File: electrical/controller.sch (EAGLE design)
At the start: 41 parts, among them IC1 555, IC2 MCP4728, Q1 DMP3098, Q2 N-CHANNEL-MOSFETSOT23-3, Q3 600mA/40V, Q4 DMP3098, U1 POLOLU_D24V22F5, U5 MCP6042, U6 MCP6042

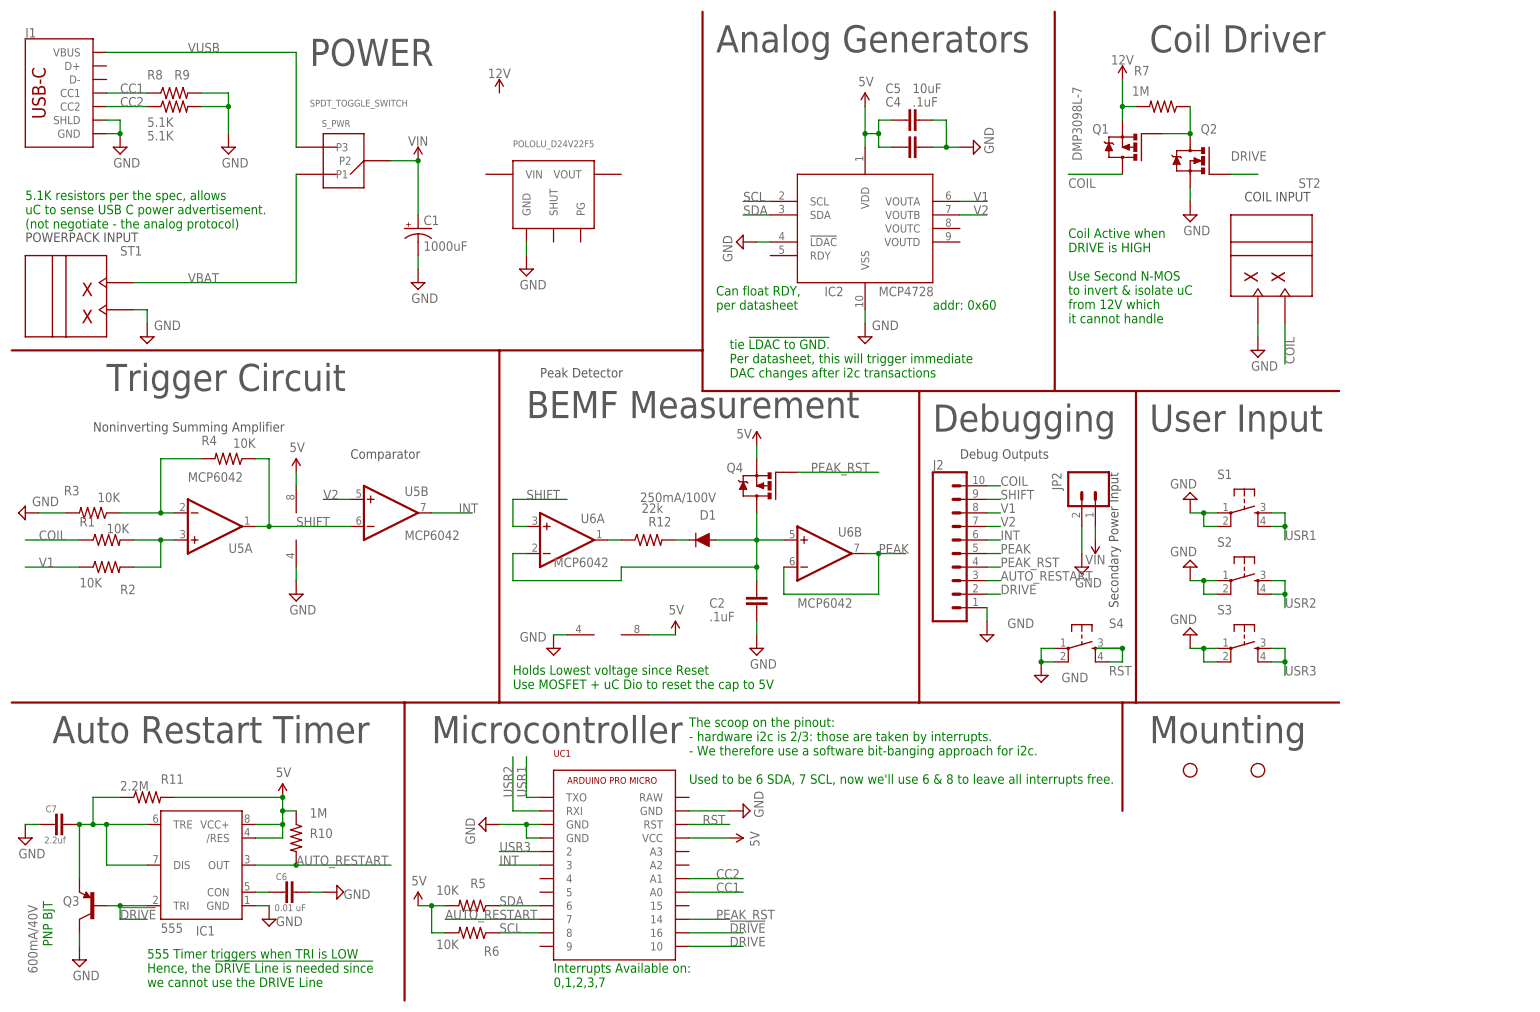
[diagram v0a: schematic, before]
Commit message: Most, but not all, of rev D2
Still need to test CC1 / CC2.
Add debug pinout silkscreen labels.
See if we can still use resistor arrays.
Calculate new values for the trigger op-amp network.
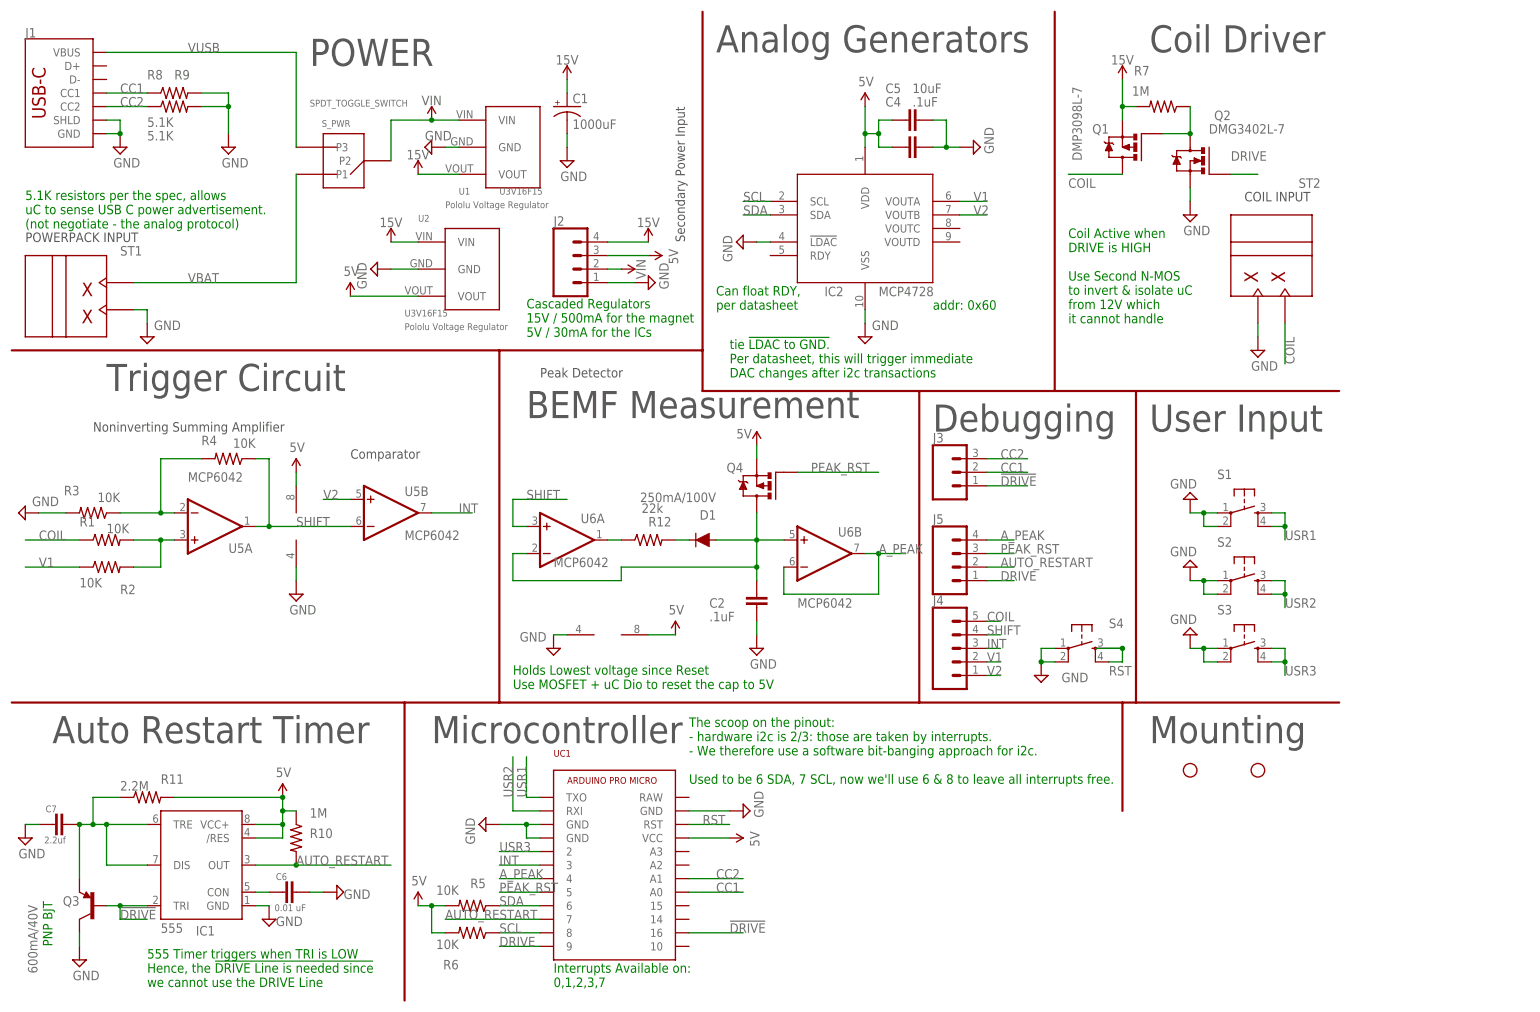
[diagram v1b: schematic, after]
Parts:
- removed JP2: (no value), pie:M02PTH
- added J3: 455-1750-1-ND, SparkFun-Connectors:CONN_03
- added J4: (no value), SparkFun-Connectors:CONN_05PTH
- added J5: (no value), SparkFun-Connectors:CONN_04PTH
- added U2: U3V16F15, BEST_Custom:POLOLU_VOLTAGE_REGULATOR_3PIN
- J2: device SparkFun-Connectors:CONN_10" -> SparkFun-Connectors:CONN_04PTH
- Q2: value N-CHANNEL-MOSFETSOT23-3 -> DMG3402L-7
- U1: value POLOLU_D24V22F5 -> U3V16F15; device BEST_Custom:POLOLU_D24V22F5 -> BEST_Custom:POLOLU_VOLTAGE_REGULATOR_3PINBOOST
- UC1: value ARDUINO_PRO_MICRO -> (none); device BEST_Custom:ARDUINO_PRO_MICRO -> BEST_Custom:ARDUINO_PRO_MICRO2D
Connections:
- removed net 12V: Q1.S, R7.2
- removed net PEAK: J2.5, U6B.-IN, U6B.OUT
- new net 15V: C1.+, J2.4, Q1.S, R7.2, U1.VOUT, U2.VIN
- new net A_PEAK: J5.4, U6B.-IN, U6B.OUT, UC1.4
- net !DRIVE: now also J3.1
- net 5V: now also J2.3, U2.VOUT
- net AUTO_RESTART: now also J5.2; no longer J2.3
- net CC1: now also J3.2
- net CC2: now also J3.3
- net COIL: now also J4.5; no longer J2.10
- net DRIVE: now also J5.1, UC1.9; no longer J2.2, UC1.10
- net GND: now also U2.GND; no longer JP2.2
- net INT: now also J4.3; no longer J2.6
- net PEAK_RST: now also J5.3, UC1.5; no longer J2.4, UC1.14
- net SHIFT: now also J4.4; no longer J2.9
- net V1: now also J4.2; no longer J2.8
- net V2: now also J4.1; no longer J2.7
- net VIN: now also J2.2, U1.VIN; no longer C1.+, JP2.1
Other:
- note added: "Cascaded Regulators 15V / 500mA for the magnet 5V / 30mA for the ICs"
- note removed: "Debug Outputs"
- note removed: "TODO: CAD & add the 12V / 5V regulators Pololu D45V1E1F5 and U3V16F12"
- moved on the sheet: C1

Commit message: Calculate resistor values for new coil
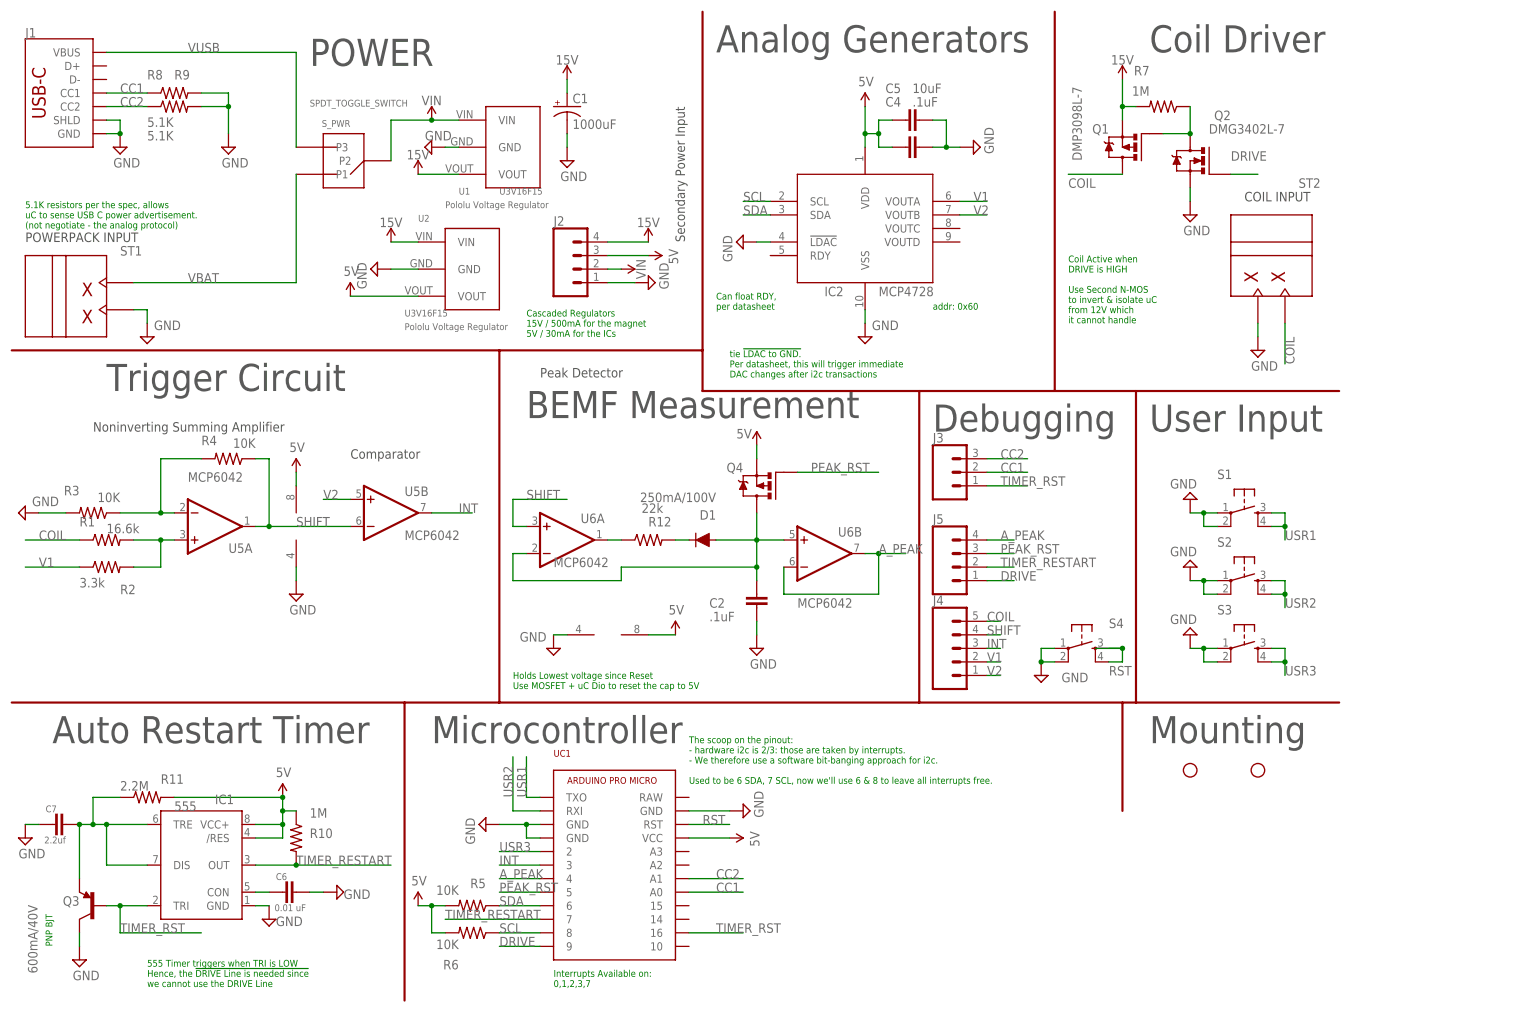
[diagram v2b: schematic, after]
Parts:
- R1: value 10K -> 16.6k
- R2: value 10K -> 3.3k
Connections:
- net !DRIVE renamed TIMER_RST
- net AUTO_RESTART renamed TIMER_RESTART
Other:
- note added: "Stage 1: V+ = R1*V1 + R2*Vcoil / (R1 + R2) Choose R1+R2 = 10k. Solve for Values by solving simultaneous equations: 1) Set Coil = 0, choose V+ = 1V ==> VShift = 2V 2) Set Coil = 3, choose V+ = 1.5V ==> VShift = 3V Previous 5V coil operation chose Coil = 1, V+ = 1.5 (approx 3x the coil count, 1/3 the gain) (Actually it's 2.69x the coil count, todo adjust later)"
- note added: "Stage 2: VShift = 1 + (R4/R3) V- VShift = 2 V-"
- note removed: "TODO: Gain math for Coil to reduce the BEMF by 3x"
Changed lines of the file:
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@@
 <part name="SUPPLY5" library="pie" deviceset="GND" device=""/>
 <part name="SUPPLY6" library="pie" deviceset="GND" device=""/>
-<part name="R2" library="pie" deviceset="R-US_" device="R0603" value="10K"/>
+<part name="R2" library="pie" deviceset="R-US_" device="R0603" value="3.3k"/>
 <part name="R3" library="pie" deviceset="R-US_" device="R0603" value="10K"/>
 <part name="R4" library="pie" deviceset="R-US_" device="R0603" value="10K"/>
@@
 <part name="U$4" library="pie" deviceset="5V" device=""/>
 <part name="SUPPLY8" library="pie" deviceset="GND" device=""/>
-<part name="R1" library="pie" deviceset="R-US_" device="R0603" value="10K"/>
+<part name="R1" library="pie" deviceset="R-US_" device="R0603" value="16.6k"/>
 <part name="SUPPLY10" library="pie" deviceset="GND" device=""/>
 <part name="C5" library="pie" deviceset="CAP" device="0805" value="10uF"/>
@@
 <wire x1="91.44" y1="55.88" x2="170.18" y2="55.88" width="0.4064" layer="94"/>
 <text x="213.36" y="48.26" size="5.08" layer="97">Mounting</text>
-<text x="101.6" y="2.54" size="1.778" layer="91">Interrupts Available on:
+<text x="101.6" y="2.54" size="1.27" layer="91">Interrupts Available on:
 0,1,2,3,7</text>
-<text x="127" y="40.64" size="1.778" layer="91">The scoop on the pinout:
+<text x="127" y="40.64" size="1.27" layer="91">The scoop on the pinout:
 - hardware i2c is 2/3: those are taken by interrupts.
 - We therefore use a software bit-banging approach for i2c.
 Used to be 6 SDA, 7 SCL, now we'll use 6 &amp; 8 to leave all interrupts free.</text>
-<text x="172.72" y="129.54" size="1.778" layer="91">addr: 0x60</text>
-<text x="2.54" y="144.78" size="1.778" layer="91">5.1K resistors per the spec, allows
+<text x="172.72" y="129.54" size="1.27" layer="91">addr: 0x60</text>
+<text x="2.54" y="144.78" size="1.27" layer="91">5.1K resistors per the spec, allows
 uC to sense USB C power advertisement.
 (not negotiate - the analog protocol)</text>
-<text x="7.62" y="10.16" size="1.778" layer="91" rot="R90">PNP BJT</text>
-<text x="134.62" y="116.84" size="1.778" layer="91">tie !LDAC to GND.
+<text x="7.62" y="10.16" size="1.27" layer="91" rot="R90">PNP BJT</text>
+<text x="134.62" y="116.84" size="1.27" layer="91">tie !LDAC to GND.
 Per datasheet, this will trigger immediate
 DAC changes after i2c transactions</text>
-<text x="132.08" y="129.54" size="1.778" layer="91">Can float RDY,
+<text x="132.08" y="129.54" size="1.27" layer="91">Can float RDY,
 per datasheet</text>
 <text x="200.66" y="157.48" size="1.778" layer="96" rot="R90">DMP3098L-7</text>
-<text x="198.12" y="127" size="1.778" layer="91">Coil Active when
+<text x="198.12" y="127" size="1.27" layer="91">Coil Active when
 DRIVE is HIGH
 Use Second N-MOS
@@
 from 12V which
 it cannot handle</text>
-<text x="25.4" y="2.54" size="1.778" layer="91">555 Timer triggers when TRI is LOW
+<text x="25.4" y="2.54" size="1.27" layer="91">555 Timer triggers when TRI is LOW
 Hence, the !DRIVE Line is needed since
 we cannot use the DRIVE Line</text>
@@
 <wire x1="195.58" y1="114.3" x2="195.58" y2="185.42" width="0.4064" layer="94"/>
 <text x="99.06" y="116.84" size="1.778" layer="97">Peak Detector</text>
-<text x="93.98" y="58.42" size="1.778" layer="91">Holds Lowest voltage since Reset
+<text x="93.98" y="58.42" size="1.27" layer="91">Holds Lowest voltage since Reset
 Use MOSFET + uC Dio to reset the cap to 5V</text>
-<text x="17.78" y="60.96" size="1.778" layer="98">TODO: Gain math for Coil to reduce the BEMF by 3x</text>
-<text x="96.52" y="124.46" size="1.778" layer="91">Cascaded Regulators
+<text x="2.54" y="58.42" size="1.27" layer="98">Stage 1:
+V+ = R1*V1 + R2*Vcoil / (R1 + R2)
+Choose R1+R2 = 10k.  Solve for Values by
+solving simultaneous equations:
+1) Set Coil = 0, choose V+ = 1V ==&gt; VShift = 2V
+2) Set Coil = 3, choose V+ = 1.5V ==&gt; VShift = 3V
+Previous 5V coil operation chose Coil = 1, V+ = 1.5 (approx 3x the coil count, 1/3 the gain)
+(Actually it's 2.69x the coil count, todo adjust later)</text>
+<text x="96.52" y="124.46" size="1.27" layer="91">Cascaded Regulators
 15V / 500mA for the magnet
 5V / 30mA for the ICs</text>
+<text x="33.02" y="76.2" size="1.27" layer="98">Stage 2:
+VShift = 1 + (R4/R3) V-
+VShift = 2 V-</text>
 </plain>
 <instances>
@@
 </instance>
 <instance part="IC1" gate="G$1" x="35.56" y="25.4" smashed="yes">
-<attribute name="NAME" x="38.1" y="13.97" size="1.778" layer="95" rot="R180"/>
-<attribute name="VALUE" x="27.94" y="12.7" size="1.778" layer="96"/>
+<attribute name="NAME" x="38.1" y="36.83" size="1.778" layer="95"/>
+<attribute name="VALUE" x="30.48" y="35.56" size="1.778" layer="96"/>
 </instance>
 <instance part="U$8" gate="G$1" x="50.8" y="38.1" smashed="yes">
@@
 <pinref part="C6" gate="G$1" pin="1"/>
 <wire x1="45.72" y1="20.32" x2="48.26" y2="20.32" width="0.1524" layer="91"/>
-</segment>
-</net>
-<net name="AUTO_RESTART" class="0">
-<segment>
-<pinref part="IC1" gate="G$1" pin="OUT"/>
-<wire x1="45.72" y1="25.4" x2="53.34" y2="25.4" width="0.1524" layer="91"/>
-<label x="53.34" y="25.4" size="1.778" layer="95"/>
-<pinref part="R10" gate="G$1" pin="2"/>
-<wire x1="53.34" y1="25.4" x2="71.12" y2="25.4" width="0.1524" layer="91"/>
-<junction x="53.34" y="25.4"/>
-</segment>
-<segment>
-<pinref part="UC1" gate="APM" pin="7"/>
-<wire x1="99.06" y1="15.24" x2="81.28" y2="15.24" width="0.1524" layer="91"/>
-<label x="81.28" y="15.24" size="1.778" layer="95"/>
-</segment>
-<segment>
-<wire x1="182.88" y1="81.28" x2="187.96" y2="81.28" width="0.1524" layer="91"/>
-<label x="185.42" y="81.28" size="1.778" layer="95"/>
-<pinref part="J5" gate="J1" pin="2"/>
 </segment>
 </net>
@@
 <wire x1="15.24" y1="33.02" x2="15.24" y2="38.1" width="0.1524" layer="91"/>
 <wire x1="15.24" y1="38.1" x2="20.32" y2="38.1" width="0.1524" layer="91"/>
-</segment>
-</net>
-<net name="!DRIVE" class="0">
-<segment>
-<pinref part="UC1" gate="APM" pin="16"/>
-<wire x1="127" y1="12.7" x2="137.16" y2="12.7" width="0.1524" layer="91"/>
-<label x="134.62" y="12.7" size="1.778" layer="95"/>
-</segment>
-<segment>
-<pinref part="IC1" gate="G$1" pin="TRI"/>
-<wire x1="20.32" y1="17.78" x2="25.4" y2="17.78" width="0.1524" layer="91"/>
-<label x="20.32" y="15.24" size="1.778" layer="95"/>
-<wire x1="20.32" y1="17.78" x2="20.32" y2="15.24" width="0.1524" layer="91"/>
-<wire x1="20.32" y1="15.24" x2="25.4" y2="15.24" width="0.1524" layer="91"/>
-<pinref part="Q3" gate="G$1" pin="B"/>
-<wire x1="20.32" y1="17.78" x2="17.78" y2="17.78" width="0.1524" layer="91"/>
-<junction x="20.32" y="17.78"/>
-</segment>
-<segment>
-<pinref part="J3" gate="J1" pin="1"/>
-<wire x1="182.88" y1="96.52" x2="190.5" y2="96.52" width="0.1524" layer="91"/>
-<label x="185.42" y="96.52" size="1.778" layer="95"/>
 </segment>
 </net>
@@
 </segment>
 </net>
+<net name="TIMER_RST" class="0">
+<segment>
+<pinref part="UC1" gate="APM" pin="16"/>
+<wire x1="127" y1="12.7" x2="137.16" y2="12.7" width="0.1524" layer="91"/>
+<label x="132.08" y="12.7" size="1.778" layer="95"/>
+</segment>
+<segment>
+<pinref part="IC1" gate="G$1" pin="TRI"/>
+<wire x1="20.32" y1="17.78" x2="25.4" y2="17.78" width="0.1524" layer="91"/>
+<label x="20.32" y="12.7" size="1.778" layer="95"/>
+<wire x1="20.32" y1="17.78" x2="20.32" y2="12.7" width="0.1524" layer="91"/>
+<wire x1="20.32" y1="12.7" x2="35.56" y2="12.7" width="0.1524" layer="91"/>
+<pinref part="Q3" gate="G$1" pin="B"/>
+<wire x1="20.32" y1="17.78" x2="17.78" y2="17.78" width="0.1524" layer="91"/>
+<junction x="20.32" y="17.78"/>
+</segment>
+<segment>
+<pinref part="J3" gate="J1" pin="1"/>
+<wire x1="182.88" y1="96.52" x2="190.5" y2="96.52" width="0.1524" layer="91"/>
+<label x="185.42" y="96.52" size="1.778" layer="95"/>
+</segment>
+</net>
+<net name="TIMER_RESTART" class="0">
+<segment>
+<pinref part="IC1" gate="G$1" pin="OUT"/>
+<wire x1="45.72" y1="25.4" x2="53.34" y2="25.4" width="0.1524" layer="91"/>
+<label x="53.34" y="25.4" size="1.778" layer="95"/>
+<pinref part="R10" gate="G$1" pin="2"/>
+<wire x1="53.34" y1="25.4" x2="71.12" y2="25.4" width="0.1524" layer="91"/>
+<junction x="53.34" y="25.4"/>
+</segment>
+<segment>
+<pinref part="UC1" gate="APM" pin="7"/>
+<wire x1="99.06" y1="15.24" x2="81.28" y2="15.24" width="0.1524" layer="91"/>
+<label x="81.28" y="15.24" size="1.778" layer="95"/>
+</segment>
+<segment>
+<wire x1="182.88" y1="81.28" x2="187.96" y2="81.28" width="0.1524" layer="91"/>
+<label x="185.42" y="81.28" size="1.778" layer="95"/>
+<pinref part="J5" gate="J1" pin="2"/>
+</segment>
+</net>
